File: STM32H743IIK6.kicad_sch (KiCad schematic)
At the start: 57 parts, among them J4 USB-C, J6 BAT, SW1 SW_Push, SW2 SW_Push, SW3 SW_Push, SW4 SW_Push, U10 STM32H743ZITx, U8 TLV75733PDBV, Y1 25MHz, Y2 32.768KHz

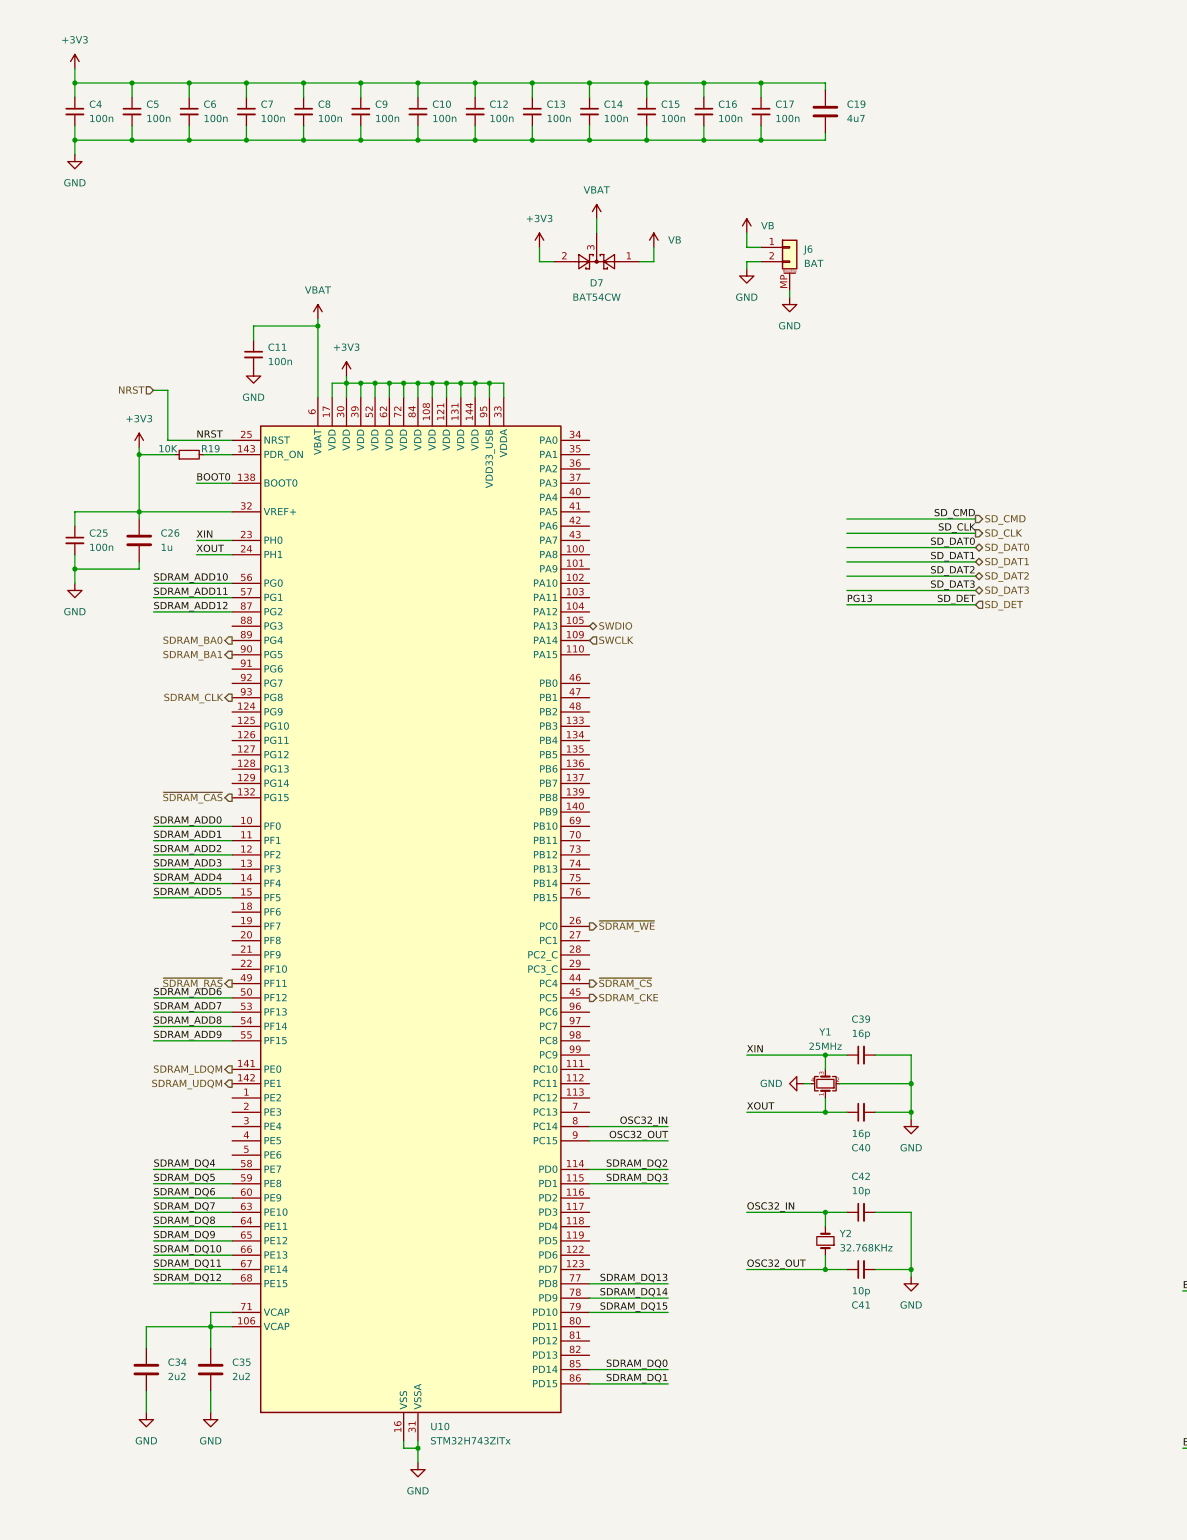
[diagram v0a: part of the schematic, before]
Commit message: Change MCU to STM32H743IIT6
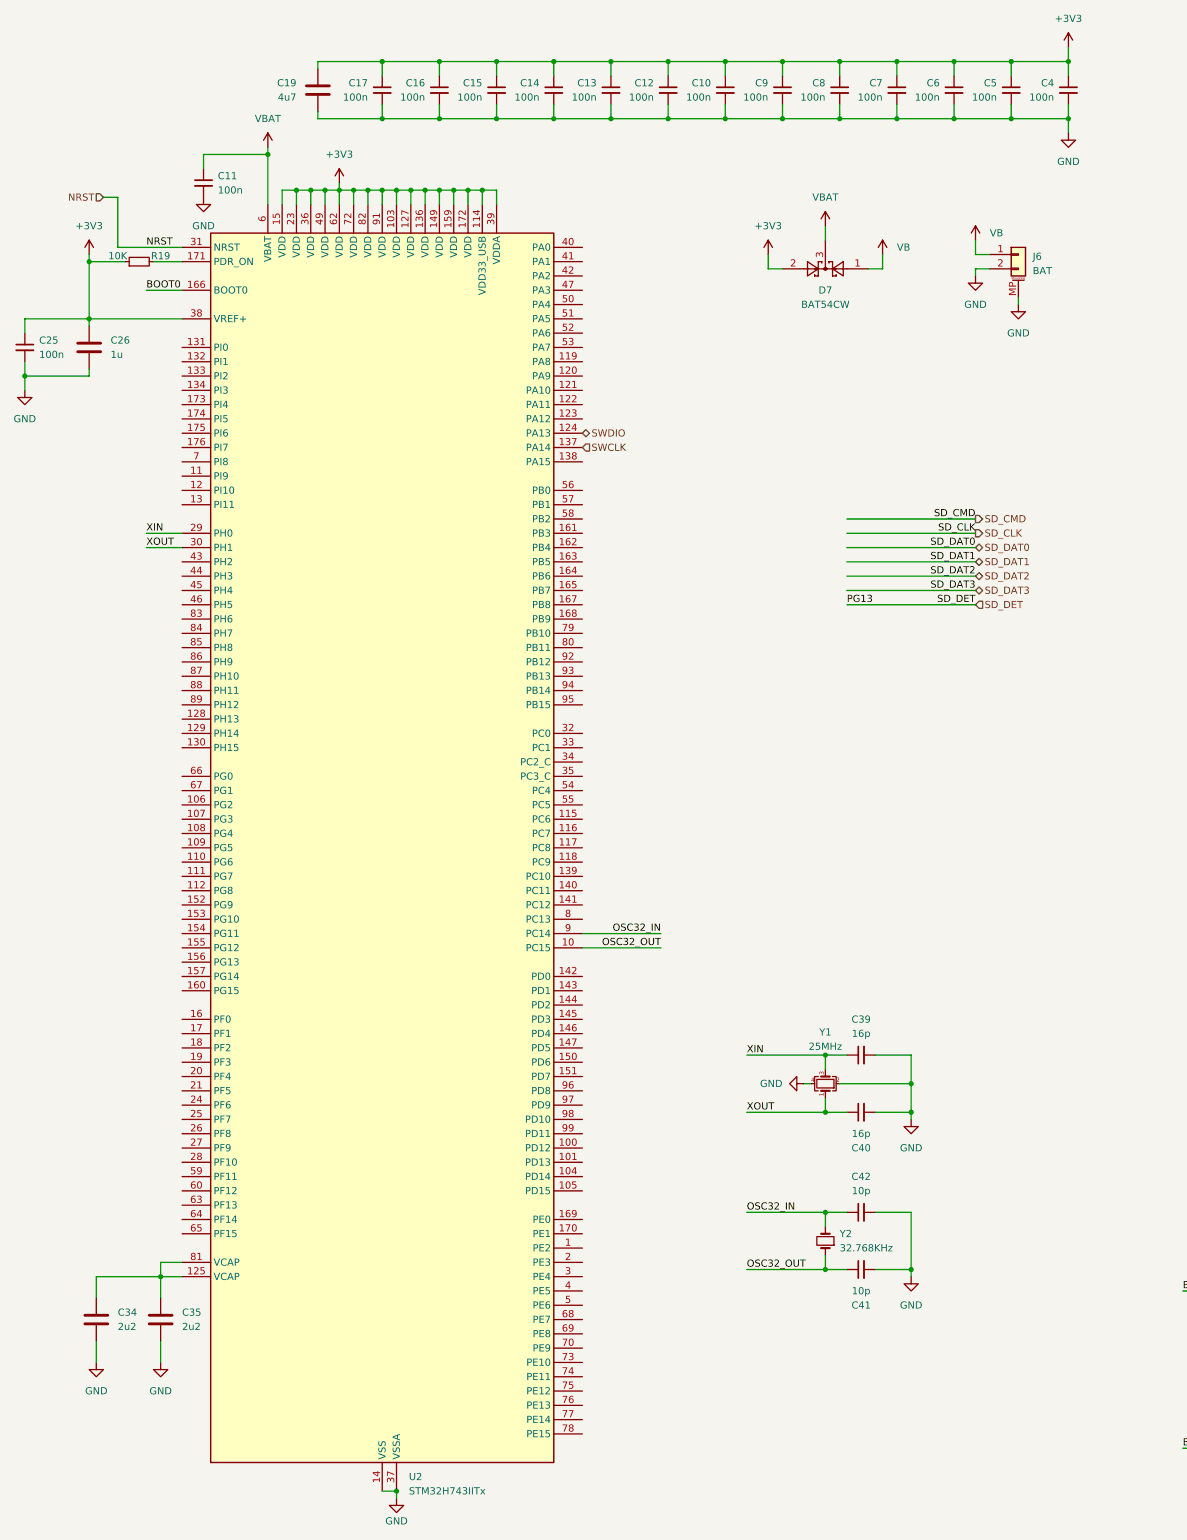
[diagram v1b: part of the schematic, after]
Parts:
- removed U10: STM32H743ZITx, Package_QFP:LQFP-144_20x20mm_P0.5mm, symbol MCU_ST_STM32H7:STM32H743ZITx
- added U2: STM32H743IITx, Package_QFP:LQFP-176_24x24mm_P0.5mm, symbol MCU_ST_STM32H7:STM32H743IITx
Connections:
- net +3V3: now also U2.103 (VDD), U2.114 (VDD33_USB), U2.127 (VDD), U2.136 (VDD), U2.149 (VDD), U2.15 (VDD), U2.159 (VDD), U2.172 (VDD), U2.23 (VDD), U2.36 (VDD), U2.38 (VREF+), U2.39 (VDDA), U2.49 (VDD), U2.62 (VDD), U2.72 (VDD), U2.82 (VDD), U2.91 (VDD)
- net BOOT0: now also U2.166 (BOOT0)
- net GND: now also U2.102 (VSS), U2.113 (VSS), U2.126 (VSS), U2.135 (VSS), U2.14 (VSS), U2.148 (VSS), U2.158 (VSS), U2.22 (VSS), U2.37 (VSSA), U2.48 (VSS), U2.61 (VSS), U2.71 (VSS), U2.90 (VSS)
- net NRST: now also U2.31 (NRST)
- net OSC32_IN: now also U2.9 (PC14)
- net OSC32_OUT: now also U2.10 (PC15)
- net SWCLK: now also U2.137 (PA14)
- net SWDIO: now also U2.124 (PA13)
- net VBAT: now also U2.6 (VBAT)
- net XIN: now also U2.29 (PH0)
- net XOUT: now also U2.30 (PH1)
- net at C34.1, C35.1: now also U2.125 (VCAP), U2.81 (VCAP)
- net at R19.2: now also U2.171 (PDR_ON)
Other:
- moved on the sheet: C10, C11, C12, C13, C14, C15, C16, C17, C19, C25, C26, C34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

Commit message: Cleaning schematic, added more independently schematics
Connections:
- net DBG_SWO: now reaches U2.161 (PB3)
- net NRST renamed DBG_NRST
- net SWCLK renamed DBG_SWCLK
- net SWDIO renamed DBG_SWDIO

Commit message: Layout SDRAM
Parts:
- removed C43: 1nF/500V, Capacitor_SMD:C_1206_3216Metric, symbol Device:C_Small
- removed D2: PRTR5V0U2X, Package_TO_SOT_SMD:SOT-143, symbol Power_Protection:PRTR5V0U2X
- removed J4: USB-C, Connector_USB:USB_C_Receptacle_G-Switch_GT-USB-7010ASV, symbol Connector:USB_C_Receptacle_USB2.0_16P
- removed R11, R12: 5K1, Resistor_SMD:R_0402_1005Metric, symbol Device:R_Small
- removed R13: 1M/0805, Resistor_SMD:R_0805_2012Metric, symbol Device:R_Small
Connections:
- net QUADSPI_BK1_NCS: now also U2.79 (PB10)
- net QUADSPI_BK2_NCS: now also U2.140 (PC11)
- net QUADSPI_CLK: now also U2.58 (PB2)
- net SDRAM_ADD0: now also U2.16 (PF0)
- net SDRAM_ADD1: now also U2.17 (PF1)
- net SDRAM_ADD10: now also U2.66 (PG0)
- net SDRAM_ADD11: now also U2.67 (PG1)
- net SDRAM_ADD12: now also U2.106 (PG2)
- net SDRAM_ADD2: now also U2.18 (PF2)
- net SDRAM_ADD3: now also U2.19 (PF3)
- net SDRAM_ADD4: now also U2.20 (PF4)
- net SDRAM_ADD5: now also U2.21 (PF5)
- net SDRAM_ADD6: now also U2.60 (PF12)
- net SDRAM_ADD7: now also U2.63 (PF13)
- net SDRAM_ADD8: now also U2.64 (PF14)
- net SDRAM_ADD9: now also U2.65 (PF15)
- net SDRAM_BA0: now also U2.108 (PG4)
- net SDRAM_BA1: now also U2.109 (PG5)
- net SDRAM_CKE: now also U2.35 (PC3_C)
- net SDRAM_CLK: now also U2.112 (PG8)
- net SDRAM_DQ0: now also U2.104 (PD14)
- net SDRAM_DQ1: now also U2.105 (PD15)
- net SDRAM_DQ10: now also U2.76 (PE13)
- net SDRAM_DQ11: now also U2.77 (PE14)
- net SDRAM_DQ12: now also U2.78 (PE15)
- net SDRAM_DQ13: now also U2.96 (PD8)
- net SDRAM_DQ14: now also U2.97 (PD9)
- net SDRAM_DQ15: now also U2.98 (PD10)
- net SDRAM_DQ2: now also U2.142 (PD0)
- net SDRAM_DQ3: now also U2.143 (PD1)
- net SDRAM_DQ4: now also U2.68 (PE7)
- net SDRAM_DQ5: now also U2.69 (PE8)
- net SDRAM_DQ6: now also U2.70 (PE9)
- net SDRAM_DQ7: now also U2.73 (PE10)
- net SDRAM_DQ8: now also U2.74 (PE11)
- net SDRAM_DQ9: now also U2.75 (PE12)
- net SDRAM_LDQM: now also U2.169 (PE0)
- net SDRAM_UDQM: now also U2.170 (PE1)
- net ~{SDRAM_CAS}: now also U2.160 (PG15)
- net ~{SDRAM_CS}: now also U2.54 (PC4)
- net ~{SDRAM_RAS}: now also U2.59 (PF11)
- net ~{SDRAM_WE}: now also U2.53 (PA7)
- net QUADSPI_BK2_IO2: now reaches U2.152 (PG9)
- net QUADSPI_BK2_IO3: now reaches U2.157 (PG14)
- net QUADSPI_BK1_IO3: now reaches U2.24 (PF6)
- net QUADSPI_BK1_IO2: now reaches U2.25 (PF7)
- net QUADSPI_BK1_IO0: now reaches U2.26 (PF8)
- net QUADSPI_BK1_IO1: now reaches U2.27 (PF9)
- net QUADSPI_BK2_IO0: now reaches U2.43 (PH2)
- net QUADSPI_BK2_IO1: now reaches U2.44 (PH3)
- no-connect marks 2 -> 0
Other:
- moved on the sheet: C39, C40, C41, C42, Y1, Y2

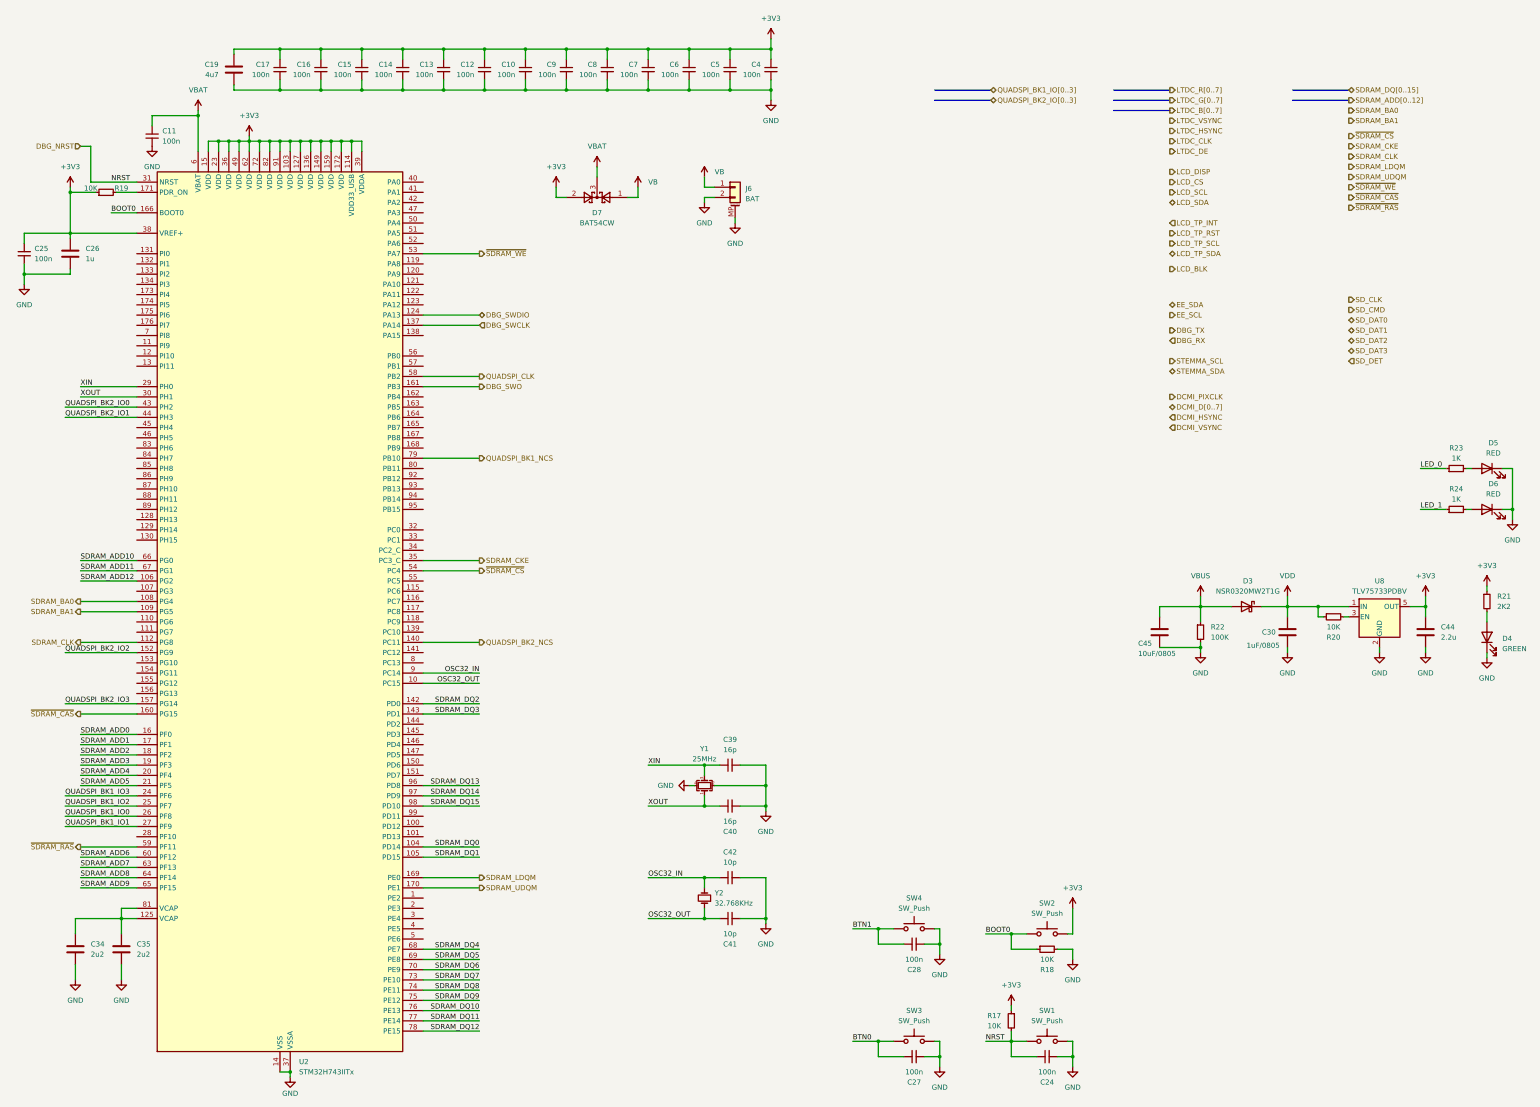
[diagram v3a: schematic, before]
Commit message: relayout SDRAM
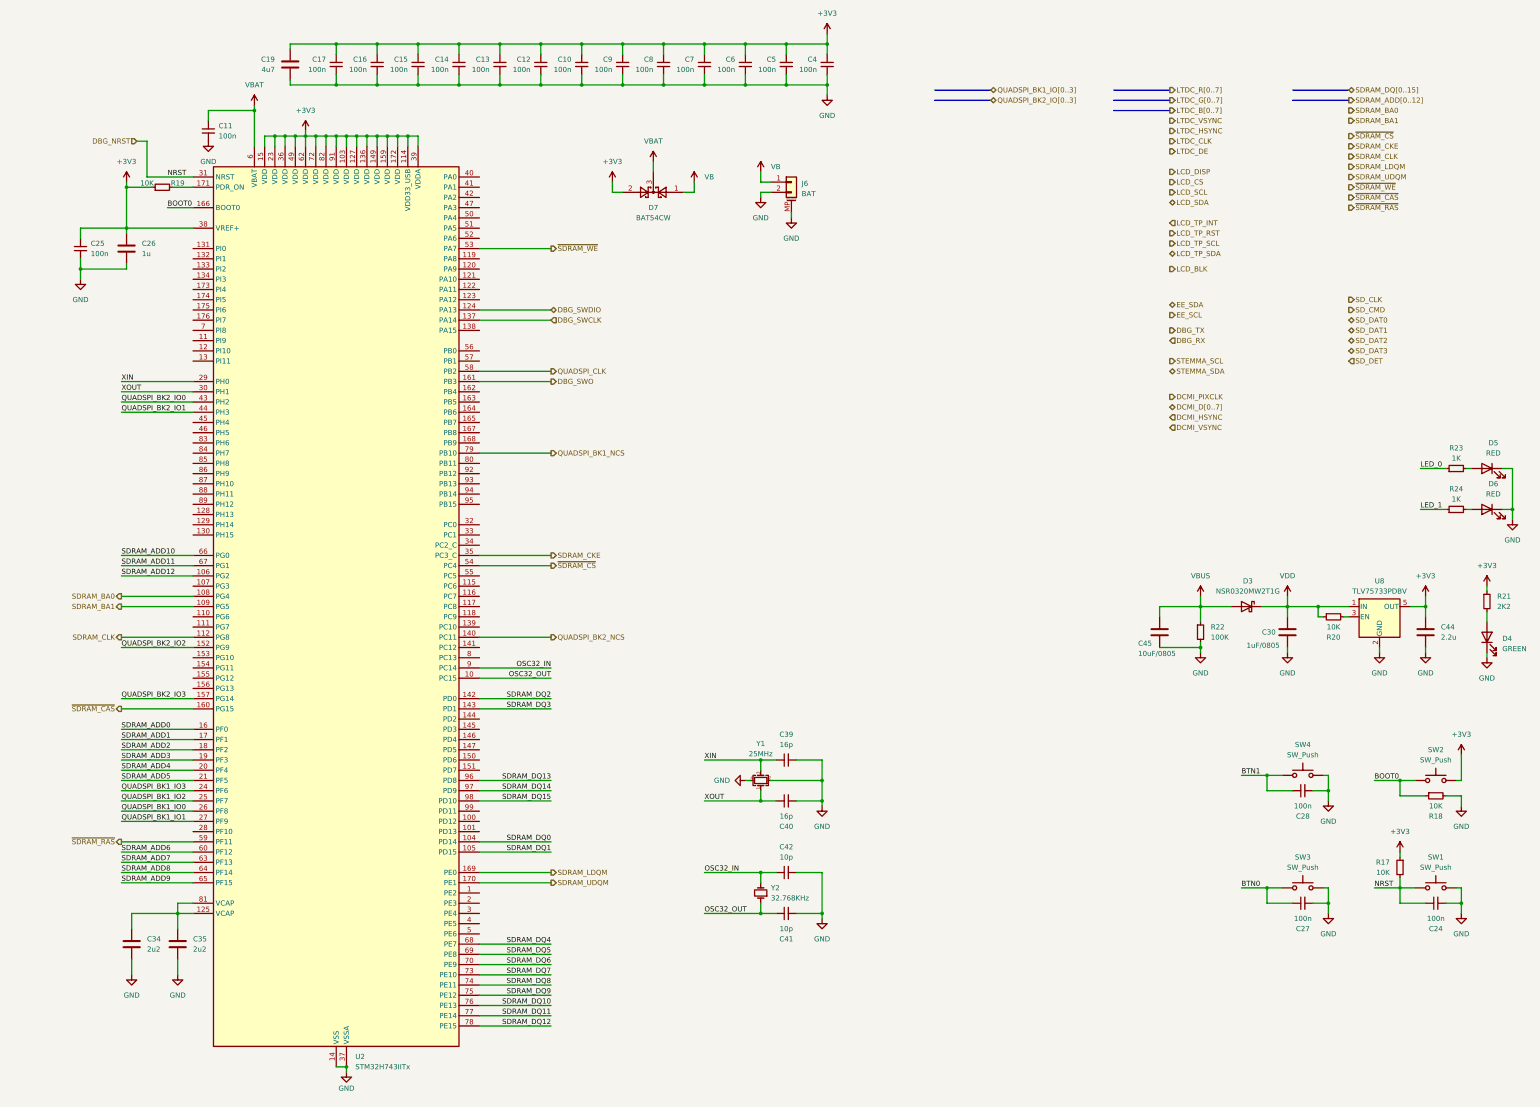
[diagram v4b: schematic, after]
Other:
- moved on the sheet: C10, C11, C12, C13, C14, C15, C16, C17, C19, C24, C25, C26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
